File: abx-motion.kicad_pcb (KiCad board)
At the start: 4 copper layers, 157 x 105 mm, 250 parts, among them J1 XT60_BAT, J102 E_STOP, J201 USB-C, J202 ENC1_CONN, J203 ENC2_CONN, J204 CAN_TERM, J205 CAN_BUS, J206 RS485_TERM, J207 RS485_BUS, J208 OLED_I2C, J209 I2C_EXP, J301 MOTOR_OUT, J401 MOTOR_OUT, J501 STEP1_MOTOR, J502 STEP1_EXT, J503 STEP2_MOTOR, J504 STEP2_EXT, J505 RELAY1_OUT, J506 RELAY2_OUT, J601 B3B-PH-K-S, J602 B3B-PH-K-S, J603 B3B-PH-K-S, J604 B3B-PH-K-S, J605 B3B-PH-K-S, J606 B3B-PH-K-S, K501 G5LE-14-DC5, K502 G5LE-14-DC5, Q1 SQJ459EP-T1_GE3, Q301 CSD18540Q5B, Q302 CSD18540Q5B, Q303 CSD18540Q5B, Q304 CSD18540Q5B, Q401 CSD18540Q5B, Q402 CSD18540Q5B, Q403 CSD18540Q5B, Q404 CSD18540Q5B, Q501 AO3400A, Q502 AO3400A, Q503 AO3400A, Q504 AO3400A, Q601 AO3400A, Q602 AO3400A, SW201 RESET, SW202 BOOT, SW203 BTN_BACK, SW204 BTN_NEXT, SW205 BTN_HOME, SW501 MICROSTEP_CFG, SW502 MICROSTEP_CFG, U1 LMR36520FADDA, U2 AP2112K-3.3, U201 USBLC6-2SC6, U202 TCAN1042V-Q1, U203 THVD1450DR, U3 ESP32-S3-WROOM-1-N8R2, U301 DRV8701ERGER, U4 74LVC14A, U401 DRV8701ERGER, U501 StepStick_DRV8825, U502 StepStick_DRV8825, U601 PCA9555PW,118

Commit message: Finalize V1.1 rear exposed-copper gold gear branding, polish, validation, and production package
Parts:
- F5: value 500mA_PTC -> 1206L050/15YR
- moved LOGO2 62.0 mm to (186.0, 138.0)
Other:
- board text added: "ABX-MOTION V1.1 — SPECS & I/O (DESIGN TARGETS)"
- board text added: "DC Servo 1&2: 2x 100W target (DRV8701E, 15A Chop)"
- board text added: "VBAT (J1 XT60): 12-32V target (25A Fuse, SMCJ30A)"
- board text removed: "ABX-MOTION V1.1 — SPECS & I/O REFERENCE"
- board text removed: "DC Servo 1&2: 2x 100W H-Bridge (DRV8701E, 15A Chop)"
- board text removed: "VBAT (J1 XT60): 12-32V (25A Fuse, Rev-Prot, SMCJ30A)"

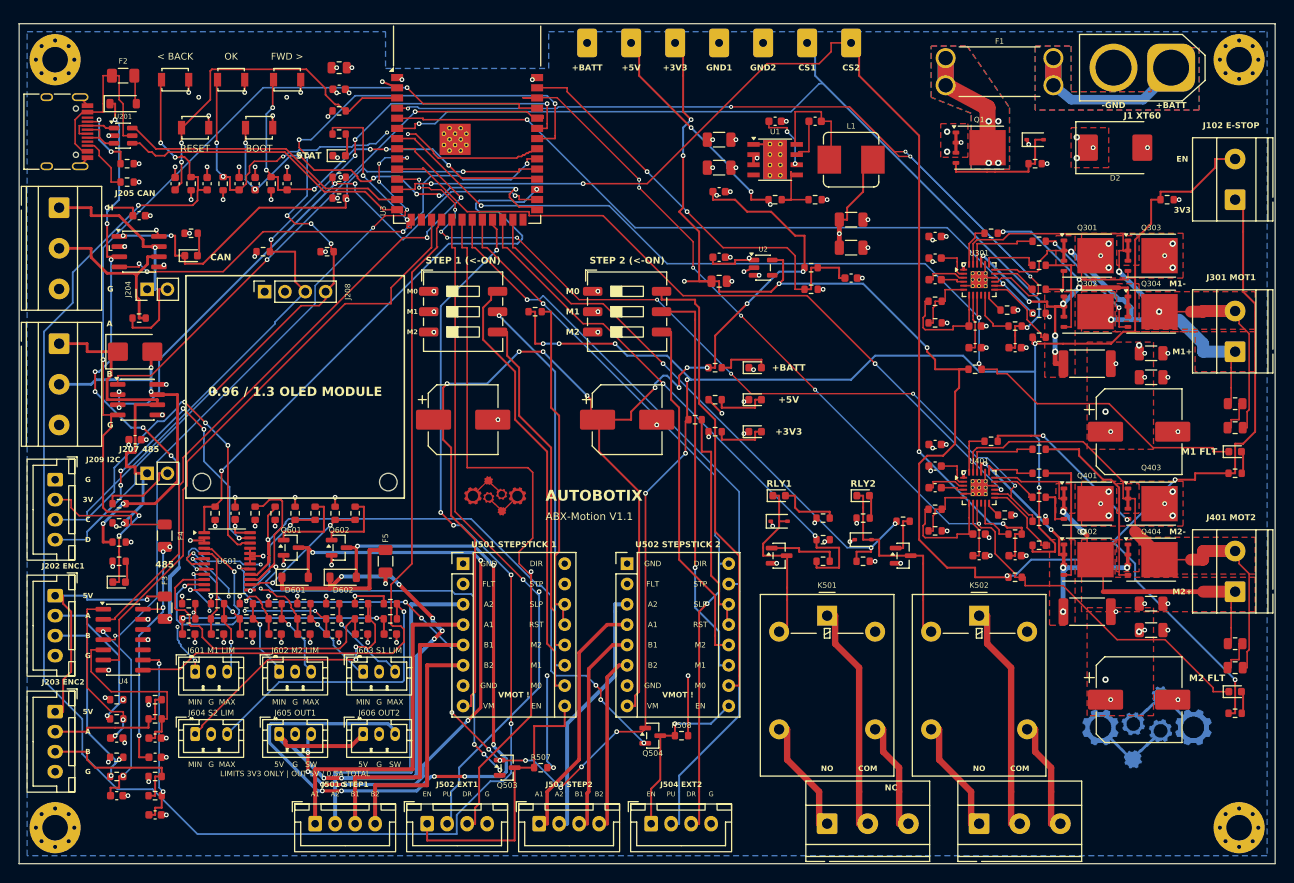
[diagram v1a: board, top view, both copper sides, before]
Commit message: Finalize Rev 1.1d robustness, thermal layout and manufacturing package
Preserve sensing and current-limit fixes, assembly part/rotation corrections,
D2 package changes, revision markings and incremental thermal copper/vias.
Archive the working checkpoints and supplier/validation evidence alongside
matched Gerbers, BOM, CPL, schematic PDF, renders and hash manifests.

Current Rev 1.1d: ERC 0; DRC 0 errors, 0 opens and 0 parity issues,
with 19 existing library footprint warnings. Preserve original routing and
component placements; physical powered qualification is not yet performed.
Relay alignment requires assembler review before assembly.
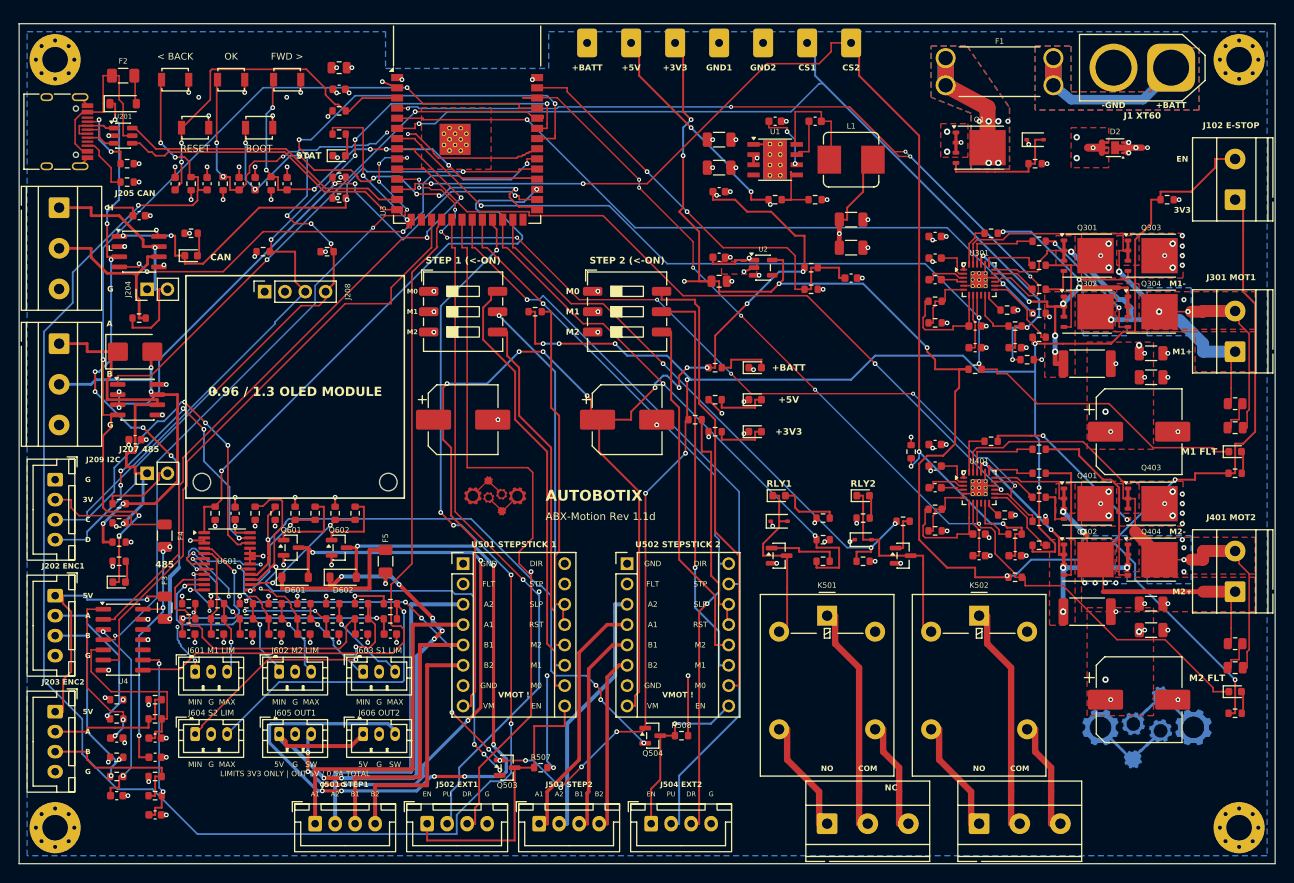
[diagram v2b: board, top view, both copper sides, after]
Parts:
- added R313: 1k, Resistor_SMD:R_0603_1608Metric, F.Cu at (171.0, 90.0)
- added R413: 1k, Resistor_SMD:R_0603_1608Metric, F.Cu at (156.5, 101.5)
- D2: value SMCJ30A -> TVS3300DRVR; footprint Diode_SMD:D_SMC -> abx-footprints:TVS3300_DRV0006A_2x2mm
- R2: value 100k -> 150k
- R302, R402: value 30k -> 12k
- R6: value 10k -> 22k
- U501, U502: footprint Module:Pololu_Breakout-16_15.2x20.3mm -> abx-footprints:StepStick_Socket_2x08_P2.54mm_D1.0
- turned D2 to 180 degrees
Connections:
- D2 pad 1: +BATT -> GND
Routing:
- net GND: track 99.3 -> 109.1 mm, vias 97 -> 102
- net /M1_CS: track 109.9 -> 116.7 mm, vias 2 -> 3
- net +BATT: track 185.8 -> 190.9 mm, vias 49 -> 57
- net /M2_CS: track 142.5 -> 145.7 mm, vias 4 -> 5
- net /Power_Supply/V_FUSED: vias 4 -> 6
- net /DC_Motor_2/MOT_OUT2: vias 0 -> 4
- net /DC_Motor_2/MOT_OUT1: vias 2 -> 6
- net /DC_Motor_1/MOT_OUT2: vias 2 -> 4
- added copper zone on B.Cu, net /DC_Motor_1/MOT_OUT1
- added copper zone on B.Cu, net /DC_Motor_1/MOT_OUT2
- added copper zone on B.Cu, net /DC_Motor_2/MOT_OUT1
- added copper zone on B.Cu, net /DC_Motor_2/MOT_OUT2
- added copper zone on F.Cu, net GND
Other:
- board text added: "ABX-MOTION REV 1.1c — SPECS & I/O (DESIGN TARGETS)"
- board text added: "ABX-Motion Rev 1.1d"
- board text added: "DC Servo 1&2: 2x 100W target (DRV8701E, 9.4A Chop)"
- board text added: "VBAT (J1 XT60): 12-32V target (25A Fuse, TVS3300)"
- board text removed: "ABX-MOTION V1.1 — SPECS & I/O (DESIGN TARGETS)"
- board text removed: "ABX-Motion V1.1"
- board text removed: "DC Servo 1&2: 2x 100W target (DRV8701E, 15A Chop)"
- board text removed: "VBAT (J1 XT60): 12-32V target (25A Fuse, SMCJ30A)"

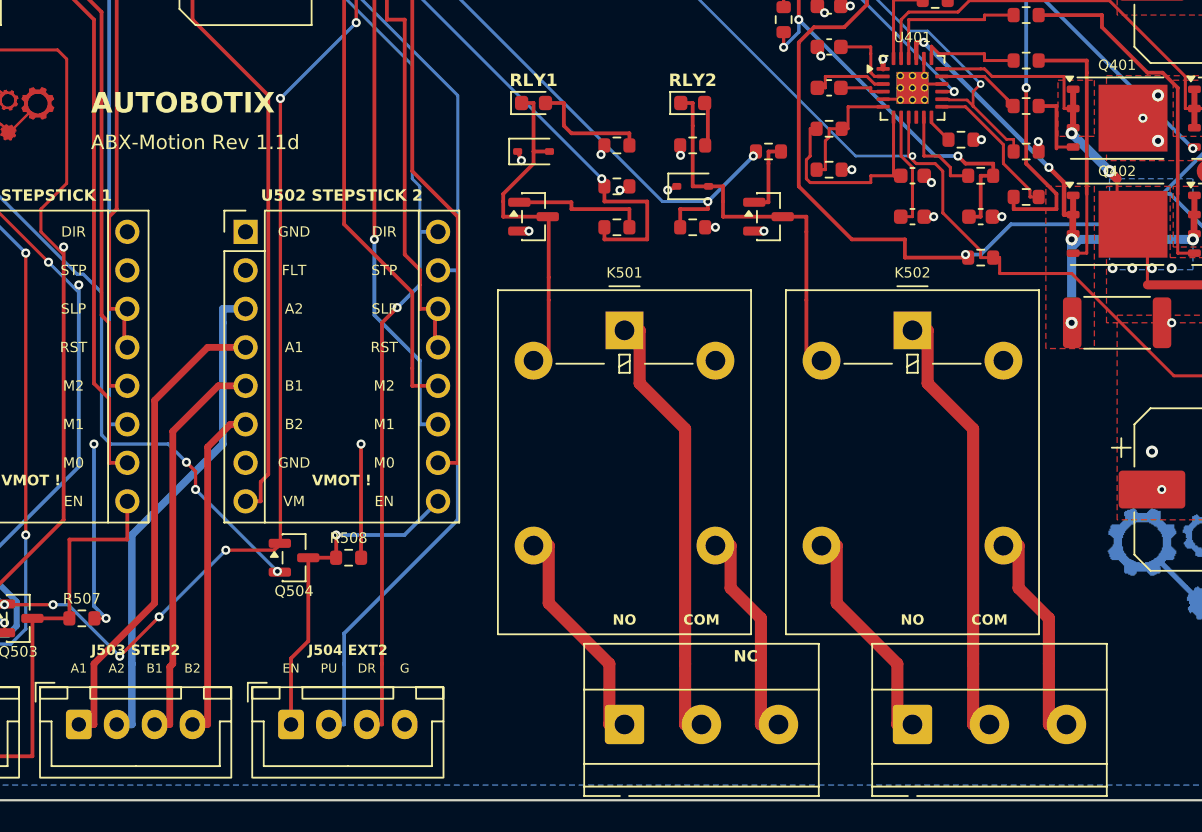
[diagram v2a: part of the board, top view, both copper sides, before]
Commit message: Consolidate Rev 1.2 relay bay and promote checked layout to root
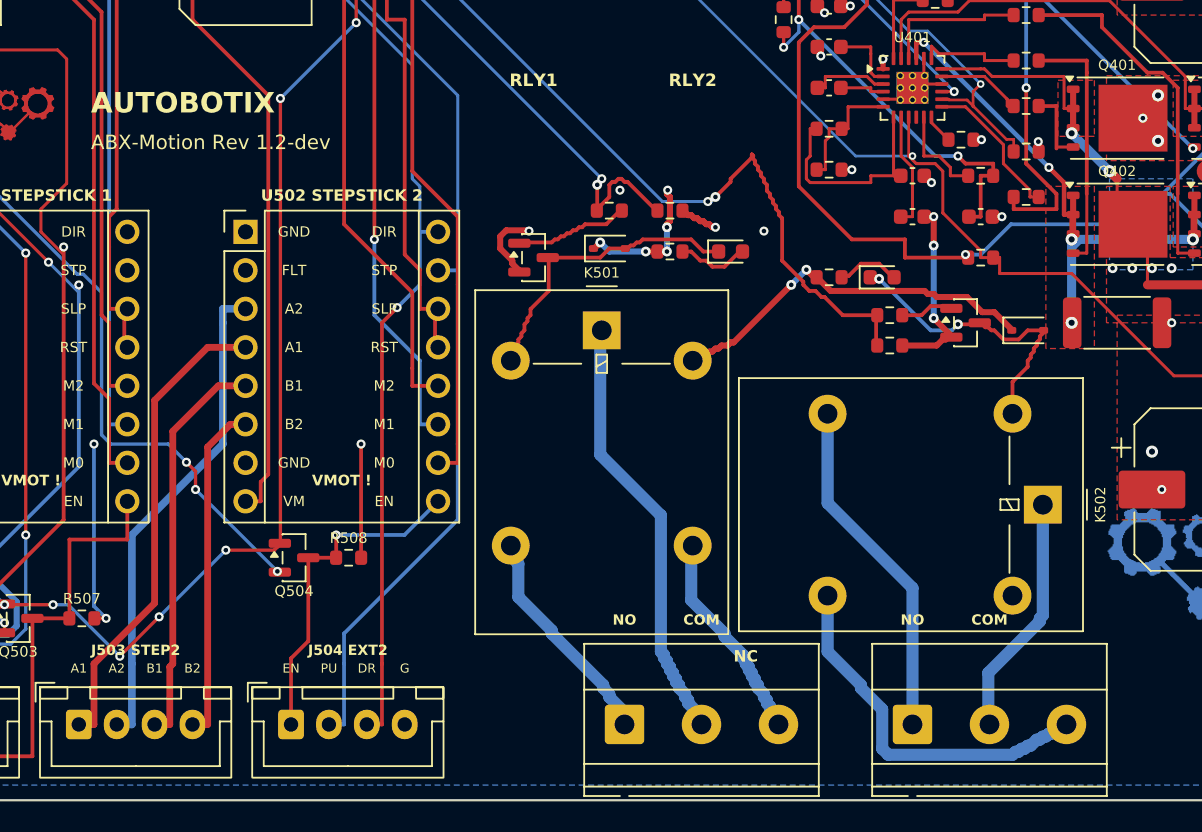
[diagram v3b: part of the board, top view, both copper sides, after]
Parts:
- moved D503 24.1 mm to (172.6, 122.0)
- moved D504 17.0 mm to (163.0, 118.5)
- moved D502 16.3 mm to (153.0, 116.8)
- moved R208 15.2 mm to (163.5, 123.0)
- moved Q502 14.8 mm to (168.5, 121.5)
- moved K502 14.4 mm to (173.6, 133.5), turned to -90 degrees
- moved R503 13.4 mm to (163.5, 121.0)
- moved R504 12.5 mm to (159.5, 118.5)
- moved D501 8.12 mm to (145.0, 116.6)
- moved R502 7.83 mm to (149.0, 116.8)
- moved R207 3.85 mm to (149.0, 114.1)
- moved Q501 2.70 mm to (140.0, 117.2)
- moved K501 1.50 mm to (144.5, 122.0)
- moved R501 1.21 mm to (145.0, 114.1)
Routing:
- net +5V: track 140.6 -> 173.3 mm, vias 25 -> 28
- net GND: track 109.1 -> 126.6 mm, vias 102 -> 104
- net /RELAY_2: track 72.1 -> 86.5 mm
- net /Steppers_and_Relays/RLY2_COM: track 29.3 -> 16.1 mm
- net /Steppers_and_Relays/RLY2_NC: track 14.8 -> 24.8 mm
- net /Steppers_and_Relays/RLY2_NO: track 15.5 -> 22.8 mm
- net /Steppers_and_Relays/RLY2_COIL_N: track 26.3 -> 20.7 mm, vias 0 -> 2
- net /Steppers_and_Relays/RLY1_COIL_N: track 23.7 -> 20.2 mm
- net /Steppers_and_Relays/RLY1_LED_A: track 8.04 -> 4.87 mm
- net /RELAY_1: track 68.1 -> 66.1 mm, vias 2 -> 3
- net /Steppers_and_Relays/RLY2_GATE: track 5.11 -> 3.67 mm
- net /Steppers_and_Relays/RLY1_GATE: track 8.91 -> 7.89 mm
- net /Steppers_and_Relays/RLY2_LED_A: track 3.59 -> 4.29 mm
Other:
- board text added: "ABX-Motion Rev 1.2-dev"
- board text added: "REV 1.2 DEVELOPMENT - RELAY BAY CANDIDATE - NOT FOR MANUFACTURE"
- board text removed: "ABX-Motion Rev 1.1d"
